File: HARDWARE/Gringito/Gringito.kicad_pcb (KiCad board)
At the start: 4 copper layers, 100 x 100.5 mm, 89 parts, among them J1 USB_C_Receptacle_PowerOnly_6P, J2 Conn_01x02, J3 Conn_01x02, U1 PTPS7A2033PDBVR, U2 INA199A1DCKR, U3 CSD97376Q4M, U4 BQ500212ARGZR, U5 CSD97376Q4M, U6 BQ51013BRHLR, U7 MCP73831T-2ATI/OT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

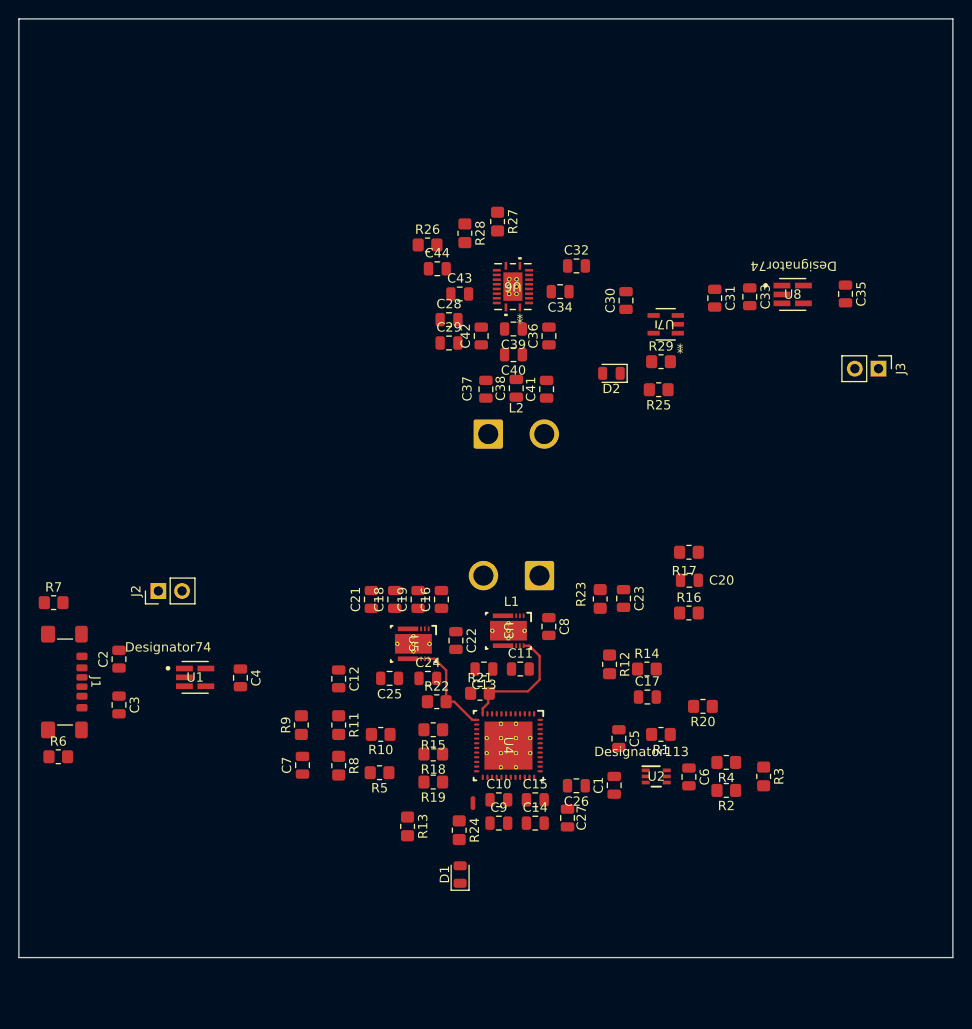
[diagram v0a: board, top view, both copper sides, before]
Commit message: V1 PCB Wireless charging
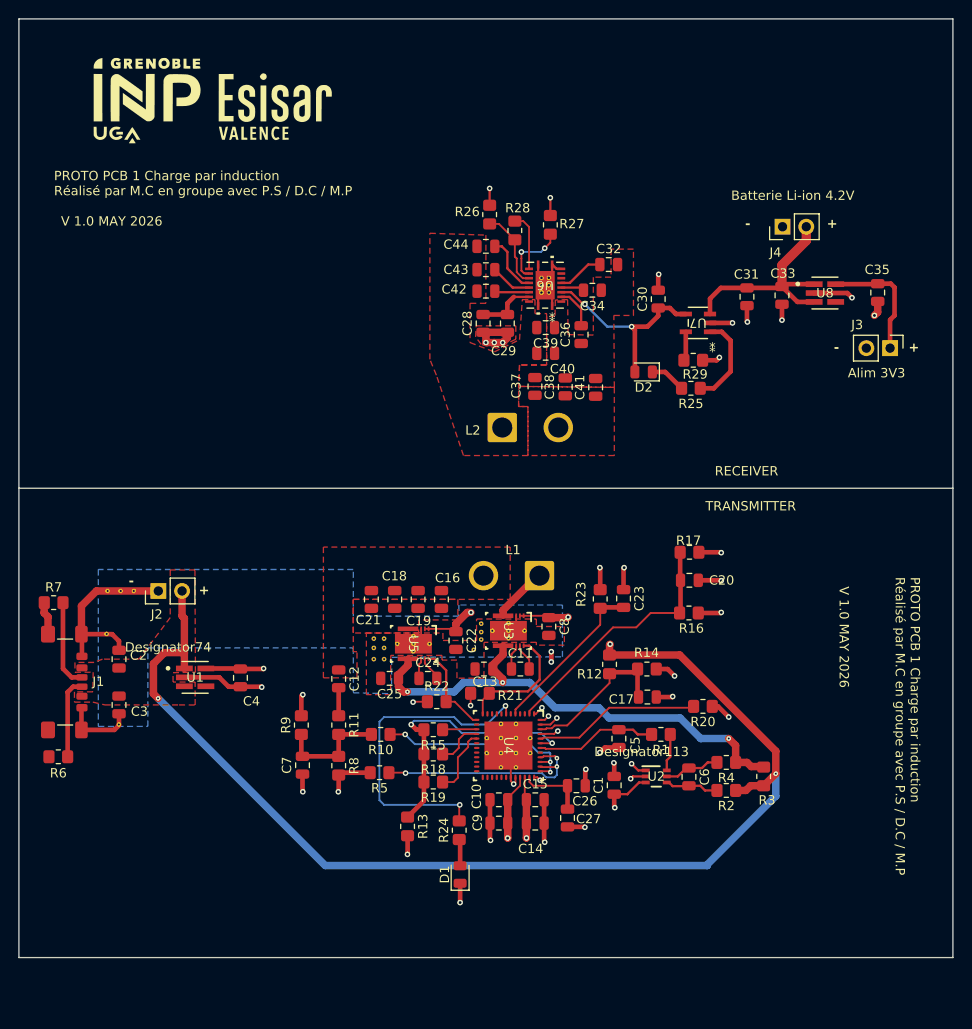
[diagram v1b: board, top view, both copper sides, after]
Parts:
- added ?: , , F.Cu at (77.9, 84.5)
- added ?: , , F.Cu at (106.1, 90.6)
- added ?: , , F.Cu at (79.3, 84.5)
- added ?: , , F.Cu at (106.1, 91.8)
- added ?: , , F.Cu at (115.7, 90.8)
- added ?: , , F.Cu at (76.4, 89.1)
- added ?: , , F.Cu at (105.0, 90.6)
- added ?: , , F.Cu at (116.5, 88.9)
- added ?: , , F.Cu at (76.5, 84.5)
- added ?: , , F.Cu at (106.1, 89.6)
- added ?: , , F.Cu at (116.5, 88.0)
- added ?: , , F.Cu at (105.0, 91.8)
- added ?: , , F.Cu at (116.5, 89.7)
- added ?: , , F.Cu at (77.7, 98.8)
- added ?: , , F.Cu at (105.0, 89.6)
- added G***: LOGO, LOGO, F.Cu at (87.8, 32.4)
- added J4: Conn_01x02, Connector_PinHeader_2.54mm:PinHeader_1x02_P2.54mm_Vertical, F.Cu at (148.8, 45.5)
- moved NT1 17.8 mm to (124.0, 91.5)
- moved R26 7.40 mm to (117.4, 44.2), turned to -90 degrees
- moved C29 6.59 mm to (119.3, 55.9), turned to 90 degrees
- moved C44 5.73 mm to (117.0, 47.6)
- moved R27 5.66 mm to (123.9, 45.3)
- moved R28 5.36 mm to (120.1, 45.9)
- moved C37 5.26 mm to (122.2, 62.6)
- moved C41 5.25 mm to (128.8, 62.7)
- moved C38 5.25 mm to (125.5, 62.6)
- moved C42 4.83 mm to (117.0, 52.4), turned to 0 degrees
- moved C43 3.82 mm to (117.0, 50.1)
- moved C28 3.67 mm to (116.7, 55.9), turned to 90 degrees
- moved U8 3.45 mm to (153.3, 52.6)
- moved C32 3.45 mm to (130.2, 49.5)
- moved C34 3.45 mm to (128.4, 52.3)
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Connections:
- C37 pad 2: AC1 -> Net-(C37-Pad2)
- C38 pad 1: AC1 -> Net-(C37-Pad2)
- C41 pad 1: AC1 -> Net-(C37-Pad2)
- L2 pad 2: AC1 -> Net-(C37-Pad2)
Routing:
- net VBUS: track 0.00 -> 137.6 mm, vias 0 -> 5
- net GNDA: track 0.00 -> 64.8 mm, vias 0 -> 26
- net /VIN_MOSFET: track 0.00 -> 52.7 mm, vias 0 -> 3
- net GND1: track 0.00 -> 37.5 mm, vias 0 -> 12
- net +3V3: track 0.00 -> 36.2 mm, vias 0 -> 9
- net /LED_A: track 0.00 -> 34.7 mm, vias 0 -> 2
- net GND: track 0.00 -> 33.8 mm, vias 0 -> 1
- net LOSS_THR: track 0.00 -> 29.3 mm, vias 0 -> 2
- net Net-(U4-T_SENSE): track 0.00 -> 27.3 mm
- net VBAT: track 0.00 -> 25.1 mm
- net /COMM-: track 0.00 -> 23.8 mm, vias 0 -> 3
- net /COMM+: track 0.00 -> 22.3 mm, vias 0 -> 3
- net OUT: track 0.00 -> 21.5 mm, vias 0 -> 2
- net Net-(U4-LED_MODE): track 0.00 -> 17.9 mm
- net Net-(U4-RESET_N): track 0.00 -> 17.6 mm
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- added copper zone on F.Cu, net AC1
- added copper zone on F.Cu, net AC2
- added copper zone on B.Cu, net GND
- added copper zone on F.Cu, net GND
- added copper zone on In1.Cu, net GND
- added copper zone on F.Cu, net GND1
- added copper zone on In1.Cu, net GNDA
- added copper zone on F.Cu, net Net-(C12-Pad1)
- added copper zone on F.Cu, net Net-(C37-Pad2)
- added copper zone on F.Cu, net Net-(U5-VSW)
- added copper zone on F.Cu, net VBUS
- added copper zone on In2.Cu, net VBUS
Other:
- outline, holes or cut-outs redrawn
- board text added: "+"
- board text added: "-"
- board text added: "Alim 3V3"
- board text added: "Batterie Li-ion 4.2V"
- board text added: "PROTO PCB 1 Charge par induction Réalisé par M.C en groupe avec P.S / D.C / M.P"
- board text added: "RECEIVER"
- board text added: "TRANSMITTER"
- board text added: "V 1.0 MAY 2026"

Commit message: V2 PCB / MODIFS DE PLAN / ERREURS
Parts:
- moved D1 1.33 mm to (115.2, 114.0), turned to 180 degrees
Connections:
- U3 pad V: (no net) -> GND
- U4 pad V: (no net) -> GNDA
- U5 pad V: (no net) -> GND
- U6 pad V: (no net) -> GND1
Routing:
- net VBUS: track 137.6 -> 140.9 mm
- net /COMM-: track 23.8 -> 24.4 mm
- net GNDA: track 64.8 -> 65.4 mm
- added copper zone on In2.Cu, net GND
- added copper zone on B.Cu, net GND1
- added copper zone on In2.Cu, net GND1
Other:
- board size 100 x 100.5 mm -> 100 x 100 mm
- board text added: "COM+"
- board text added: "COM-"

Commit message: final version + bom
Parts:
- C16, C18, C19, C21: footprint Capacitor_SMD:C_0805_2012Metric -> Capacitor_SMD:C_1206_3216Metric_Pad1.33x1.80mm_HandSolder
- moved C21 1.40 mm to (103.5, 84.8)
- moved C18 0.99 mm to (106.5, 84.8)
- moved C16 0.71 mm to (112.5, 84.8)
- moved C19 0.70 mm to (109.5, 84.8)
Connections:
- U3 pad V: GND -> (no net)
- U4 pad V: GNDA -> (no net)
- U5 pad V: GND -> (no net)
- U6 pad V: GND1 -> (no net)
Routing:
- net /VIN_MOSFET: track 52.7 -> 55.7 mm
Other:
- outline, holes or cut-outs redrawn

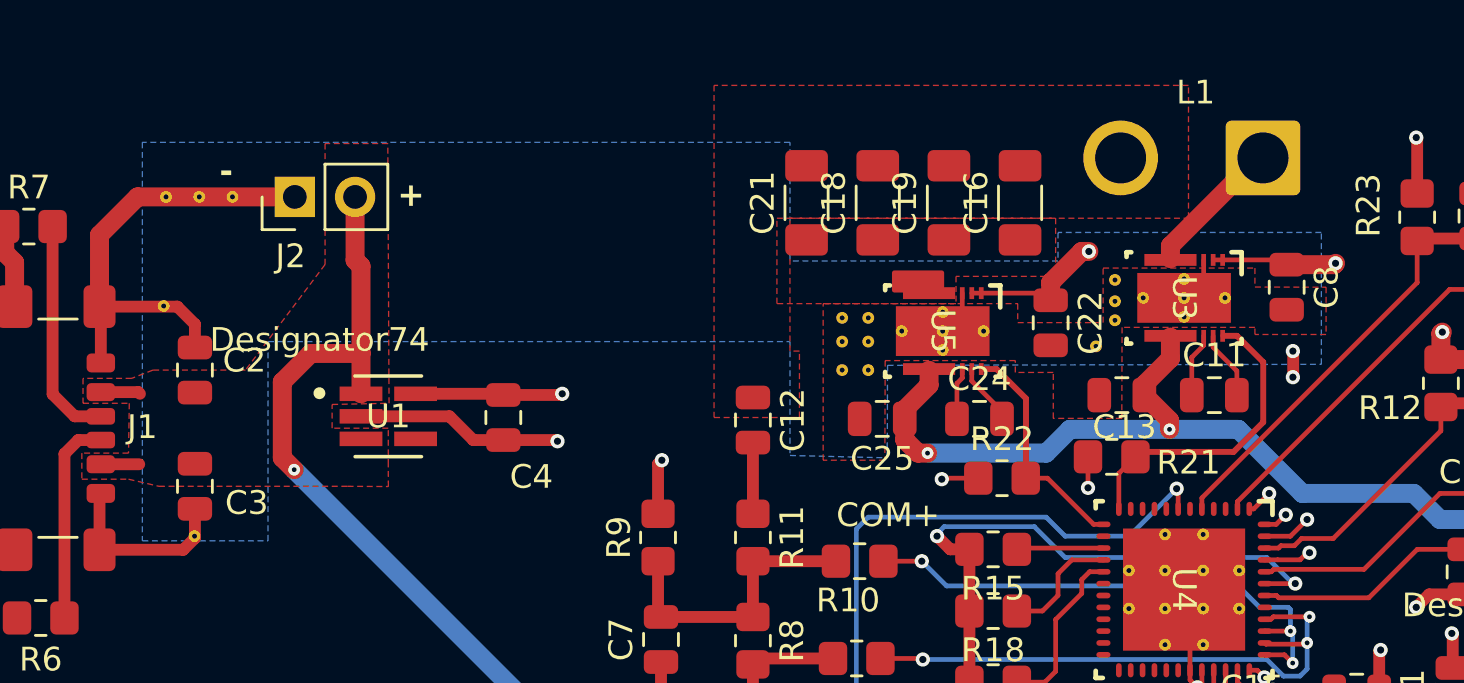
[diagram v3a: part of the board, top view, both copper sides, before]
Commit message: corrections via pas au bon potentiel
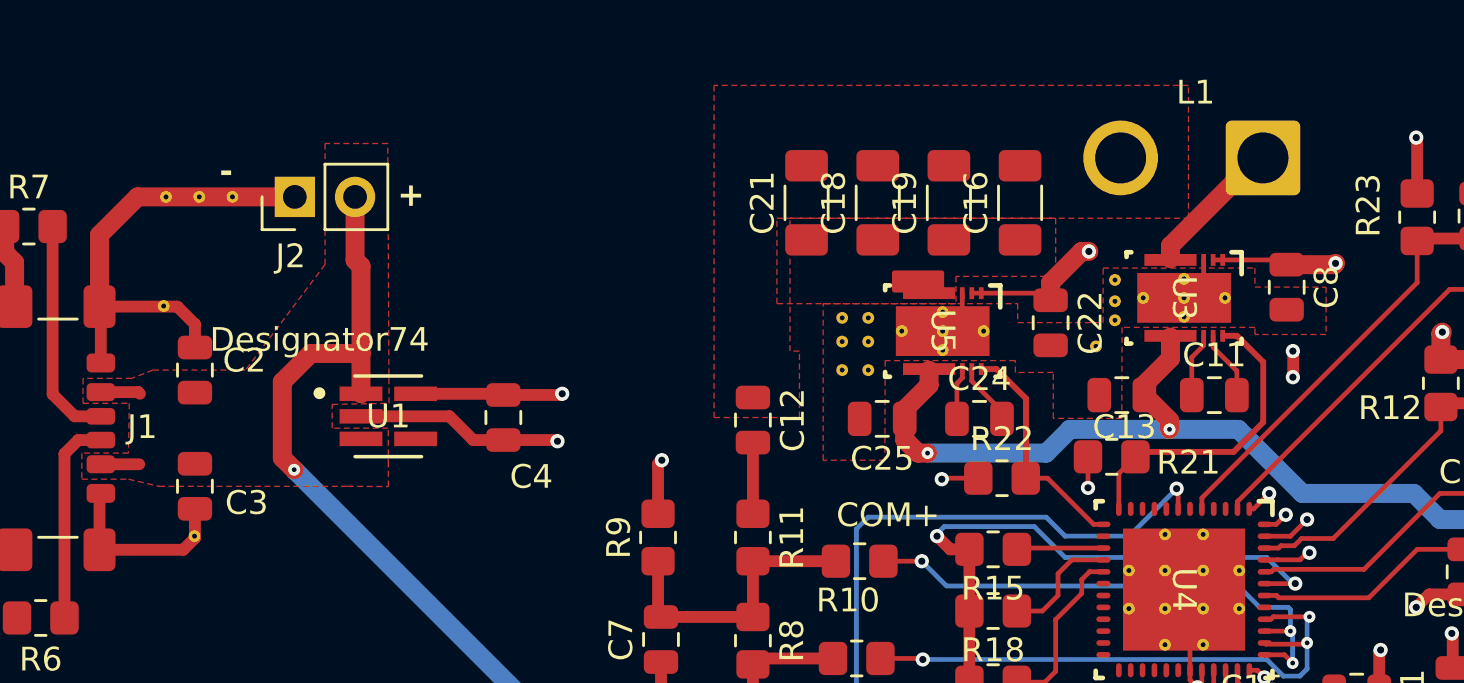
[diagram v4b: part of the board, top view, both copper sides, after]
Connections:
- U3 pad V: (no net) -> GND
- U4 pad V: (no net) -> GNDA
- U5 pad V: (no net) -> GND
- U6 pad V: (no net) -> GND1
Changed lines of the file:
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@@
 			(layers "*.Cu" "*.Mask")
 			(remove_unused_layers no)
+			(net 3 "GND")
 		)
 		(pad "V" thru_hole circle
@@
 			(layers "*.Cu" "*.Mask")
 			(remove_unused_layers no)
+			(net 3 "GND")
 		)
 		(pad "V" thru_hole circle
@@
 			(layers "*.Cu" "*.Mask")
 			(remove_unused_layers no)
+			(net 3 "GND")
 		)
 		(pad "V" thru_hole circle
@@
 			(layers "*.Cu" "*.Mask")
 			(remove_unused_layers no)
+			(net 3 "GND")
 		)
 		(pad "V" thru_hole circle
@@
 			(layers "*.Cu" "*.Mask")
 			(remove_unused_layers no)
+			(net 3 "GND")
 		)
 		(embedded_fonts no)
@@
 			(layers "*.Cu" "*.Mask")
 			(remove_unused_layers no)
+			(net 21 "GND1")
 		)
 		(pad "V" thru_hole circle
@@
 			(layers "*.Cu" "*.Mask")
 			(remove_unused_layers no)
+			(net 21 "GND1")
 		)
 		(pad "V" thru_hole circle
@@
 			(layers "*.Cu" "*.Mask")
 			(remove_unused_layers no)
+			(net 21 "GND1")
 		)
 		(pad "V" thru_hole circle
@@
 			(layers "*.Cu" "*.Mask")
 			(remove_unused_layers no)
+			(net 21 "GND1")
 		)
 		(pad "V" thru_hole circle
@@
 			(layers "*.Cu" "*.Mask")
 			(remove_unused_layers no)
+			(net 21 "GND1")
 		)
 		(embedded_fonts no)
@@
 			(layers "*.Cu" "*.Mask")
 			(remove_unused_layers no)
+			(net 3 "GND")
 		)
 		(pad "V" thru_hole circle
@@
 			(layers "*.Cu" "*.Mask")
 			(remove_unused_layers no)
+			(net 3 "GND")
 		)
 		(pad "V" thru_hole circle
@@
 			(layers "*.Cu" "*.Mask")
 			(remove_unused_layers no)
+			(net 3 "GND")
 		)
 		(pad "V" thru_hole circle
@@
 			(layers "*.Cu" "*.Mask")
 			(remove_unused_layers no)
+			(net 3 "GND")
 		)
 		(pad "V" thru_hole circle
@@
 			(layers "*.Cu" "*.Mask")
 			(remove_unused_layers no)
+			(net 3 "GND")
 		)
 		(embedded_fonts no)
@@
 			(layers "*.Cu" "*.Mask")
 			(remove_unused_layers no)
+			(net 2 "GNDA")
 		)
 		(pad "V" thru_hole circle
@@
 			(layers "*.Cu" "*.Mask")
 			(remove_unused_layers no)
+			(net 2 "GNDA")
 		)
 		(pad "V" thru_hole circle
@@
 			(layers "*.Cu" "*.Mask")
 			(remove_unused_layers no)
+			(net 2 "GNDA")
 		)
 		(pad "V" thru_hole circle
@@
 			(layers "*.Cu" "*.Mask")
 			(remove_unused_layers no)
+			(net 2 "GNDA")
 		)
 		(pad "V" thru_hole circle
@@
 			(layers "*.Cu" "*.Mask")
 			(remove_unused_layers no)
+			(net 2 "GNDA")
 		)
 		(pad "V" thru_hole circle
@@
 			(layers "*.Cu" "*.Mask")
 			(remove_unused_layers no)
+			(net 2 "GNDA")
 		)
 		(pad "V" thru_hole circle
@@
 			(layers "*.Cu" "*.Mask")
 			(remove_unused_layers no)
+			(net 2 "GNDA")
 		)
 		(pad "V" thru_hole circle
@@
 			(layers "*.Cu" "*.Mask")
 			(remove_unused_layers no)
+			(net 2 "GNDA")
 		)
 		(pad "V" thru_hole circle
@@
 			(layers "*.Cu" "*.Mask")
 			(remove_unused_layers no)
+			(net 2 "GNDA")
 		)
 		(pad "V" thru_hole circle
@@
 			(layers "*.Cu" "*.Mask")
 			(remove_unused_layers no)
+			(net 2 "GNDA")
 		)
 		(pad "V" thru_hole circle
@@
 			(layers "*.Cu" "*.Mask")
 			(remove_unused_layers no)
+			(net 2 "GNDA")
 		)
 		(pad "V" thru_hole circle
@@
 			(layers "*.Cu" "*.Mask")
 			(remove_unused_layers no)
+			(net 2 "GNDA")
 		)
 		(embedded_fonts no)
@@
 			)
 		)
-	)
-	(zone
-		(net 3)
-		(net_name "GND")
-		(layer "B.Cu")
-		(hatch edge 0.5)
-		(priority 10)
-		(connect_pads
-			(clearance 0.5)
-		)
-		(min_thickness 0.25)
-		(filled_areas_thickness no)
-		(fill yes
-			(thermal_gap 0.5)
-			(thermal_bridge_width 0.5)
-		)
-		(polygon
-			(pts
-				(xy 75.5 82.2) (xy 75.5 99) (xy 80.8 99) (xy 80.8 90.6) (xy 102.8 90.6) (xy 102.8 95.4) (xy 106.9 95.5)
-				(xy 106.913996 91.6) (xy 125.2 91.557002) (xy 125.2 86) (xy 114.1 86) (xy 114.1 87.2) (xy 102.8 87.2)
-				(xy 102.8 82.2)
-			)
-		)
